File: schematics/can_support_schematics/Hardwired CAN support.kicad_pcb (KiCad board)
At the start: 2 copper layers, 39 parts, among them J1 Conn_01x05_Female, J2 Conn_01x05_Male, J3 Conn_01x05_Male, J4 Screw_Terminal_01x04, J5 Screw_Terminal_01x02, J6 Screw_Terminal_01x02, J7 Screw_Terminal_01x02, Q1 MMBF170, SW1 SW_DIP_x04, U1 SPST_POWER_RELAY, U2 PIC18F26K83, U3 MCP2562, Y1 Crystal

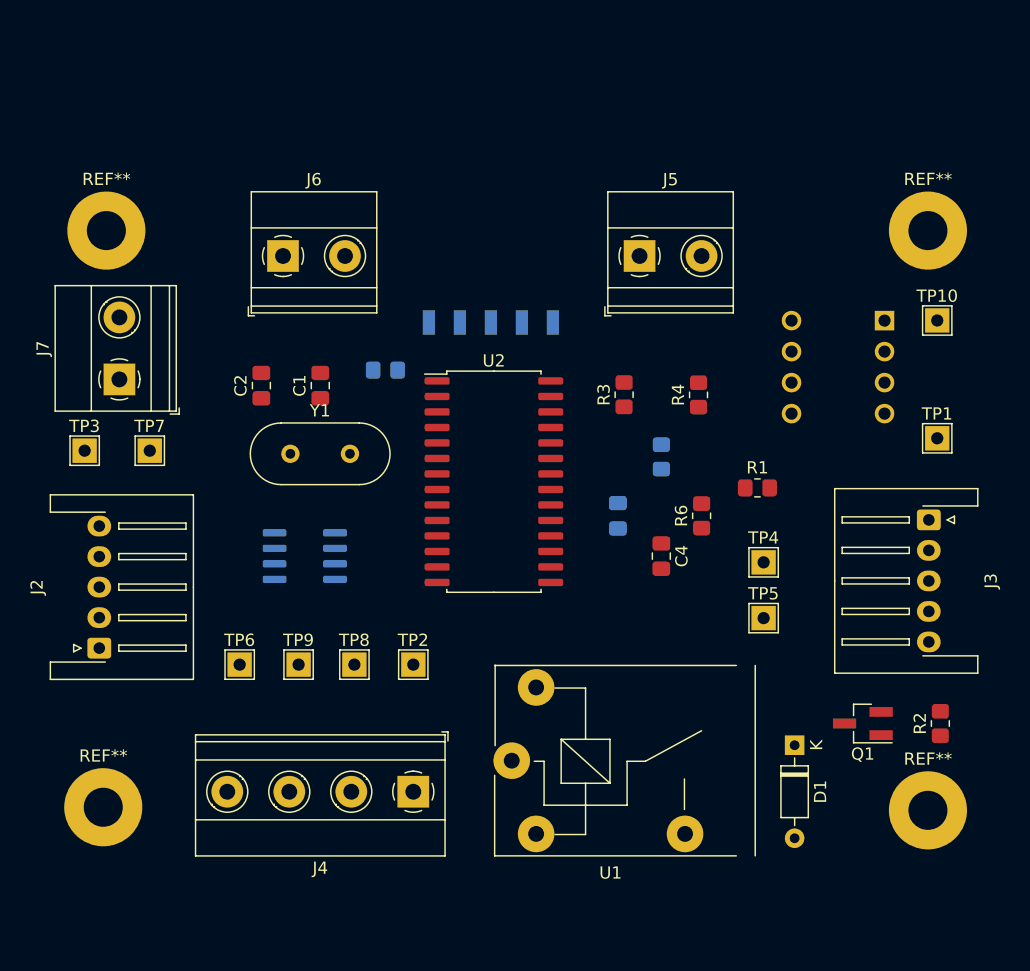
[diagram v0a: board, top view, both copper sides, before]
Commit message: Finished routing board
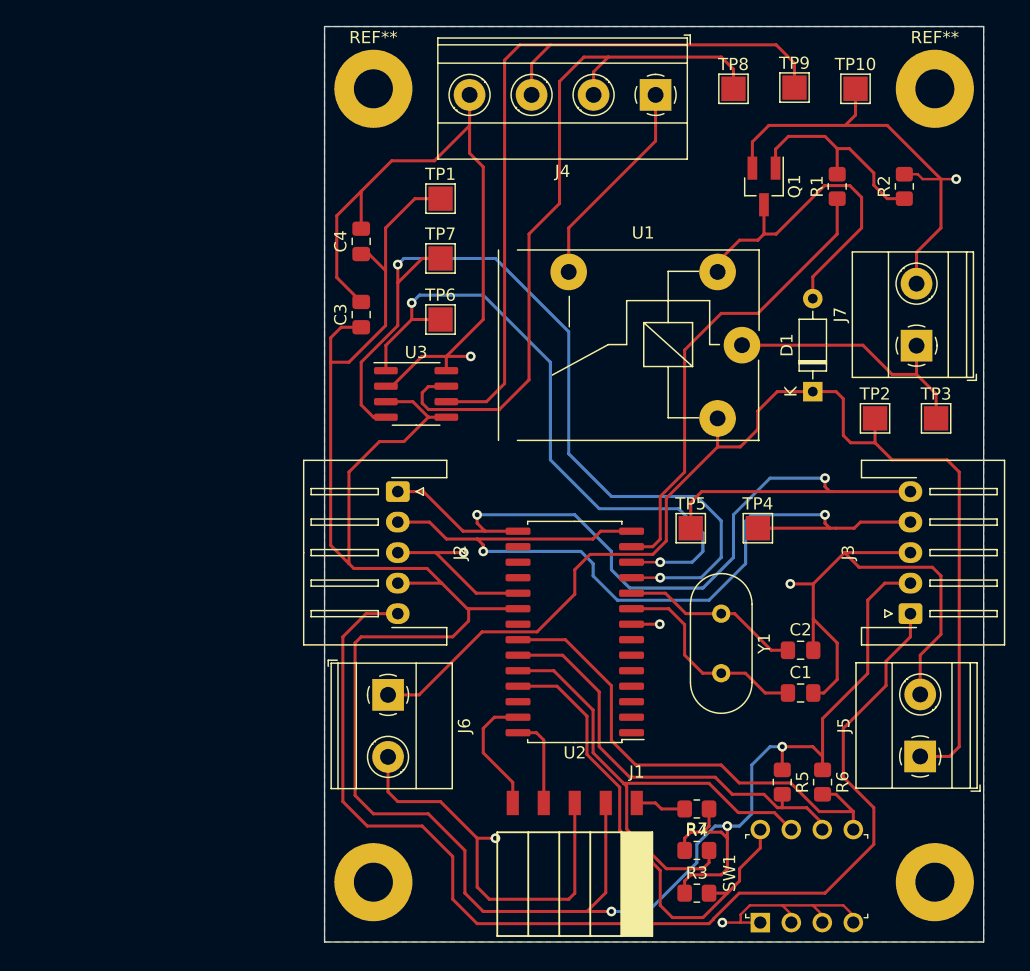
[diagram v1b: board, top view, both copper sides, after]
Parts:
- C3, J1, R5, R7, SW1, U3: moved to F.Cu
- moved TP3 69.8 mm to (171.1, 92.6)
- moved J7 65.4 mm to (169.5, 86.6)
- moved TP9 62.3 mm to (159.5, 65.5)
- moved J4 60.4 mm to (148.1, 66.1)
- moved TP8 56.5 mm to (154.5, 65.6)
- moved SW1 50.4 mm to (156.7, 133.9), turned to 90 degrees
- moved C2 49.2 mm to (160.0, 111.6), turned to 0 degrees
- moved J5 47.0 mm to (169.8, 120.3), turned to 90 degrees
- moved C1 46.7 mm to (160.0, 115.1), turned to 0 degrees
- moved TP1 45.2 mm to (130.5, 74.6)
- moved Q1 44.7 mm to (157.0, 73.6), turned to -90 degrees
- moved R2 44.1 mm to (168.5, 73.6)
- moved R7 44.1 mm to (151.5, 124.6), turned to 180 degrees
- moved TP2 42.9 mm to (166.1, 92.6)
- moved R3 41.3 mm to (151.5, 131.5), turned to 0 degrees
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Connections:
- J1 pad 1: /ICSPCLK -> /MCLR
- J1 pad 2: /ICSPDAT -> +5V
- J1 pad 4: +5V -> /ICSPDAT
- J1 pad 5: /MCLR -> /ICSPCLK
- U2 pad 13: unconnected-(U2-Pad13) -> /TRIG_PIN
- U2 pad 21: /TRIG_PIN -> unconnected-(U2-Pad21)
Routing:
- net +5V: track 0.00 -> 208.1 mm, vias 0 -> 3
- net GND: track 0.00 -> 204.9 mm, vias 0 -> 7
- net +12V: track 0.00 -> 96.0 mm
- net Net-(J2-Pad5): track 0.00 -> 93.4 mm
- net /SDA: track 0.00 -> 72.2 mm, vias 0 -> 2
- net /CAN_RX: track 0.00 -> 72.0 mm, vias 0 -> 2
- net /SCL: track 0.00 -> 70.4 mm, vias 0 -> 2
- net /CAN_L: track 0.00 -> 63.6 mm
- net /CAN_H: track 0.00 -> 59.2 mm
- net /CAN_TX: track 0.00 -> 53.4 mm, vias 0 -> 2
- net /DIP_2: track 0.00 -> 43.0 mm
- net /DIP_4: track 0.00 -> 40.5 mm
- net /DIP_1: track 0.00 -> 39.2 mm
- net /TRIG_PIN: track 0.00 -> 38.3 mm
- net /DIP_3: track 0.00 -> 34.9 mm
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- added copper zone on B.Cu, net GND
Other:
- board outline added: 54 x 75 mm

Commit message: Updated recommended changes to PCB
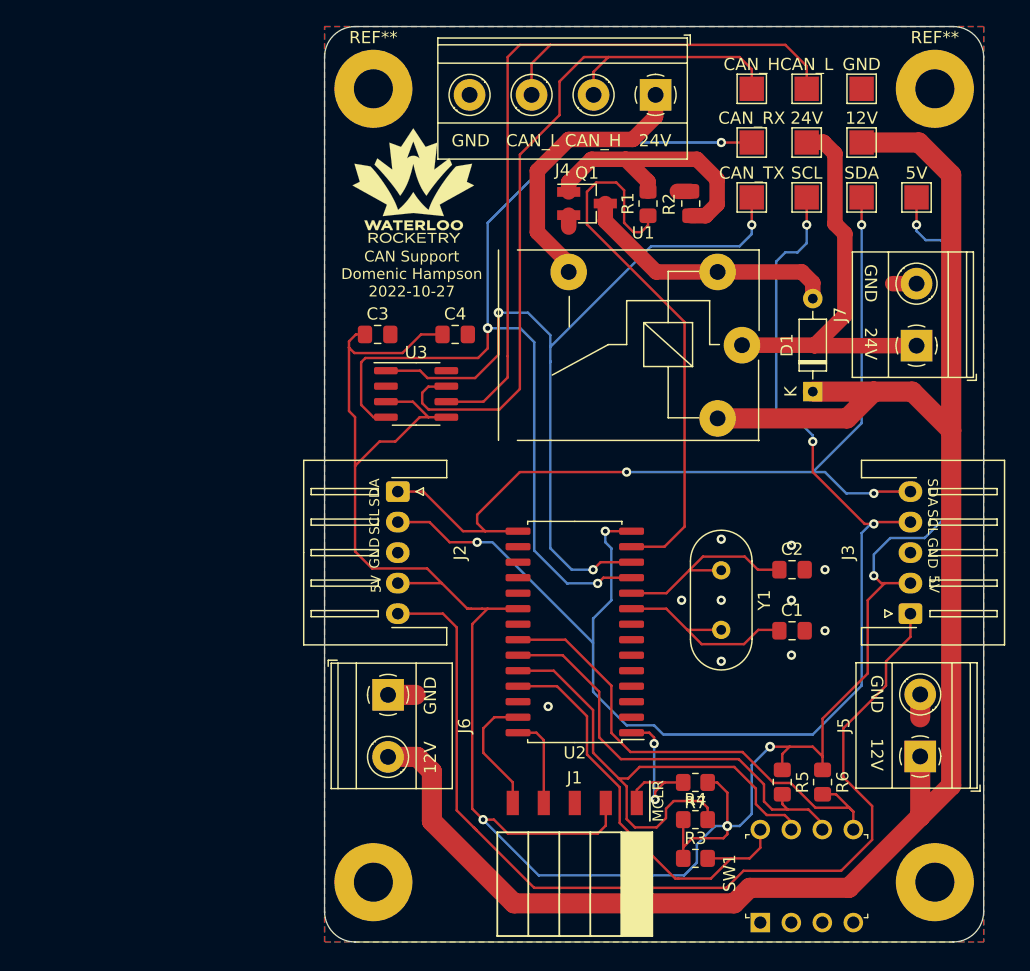
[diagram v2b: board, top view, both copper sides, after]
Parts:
- added G***: LOGO, custom:rocketry_logo_small, F.Cu at (128.3, 73.5)
- moved 5V 39.0 mm to (169.5, 74.5)
- moved SDA 30.5 mm to (165.0, 74.5)
- moved SCL 27.4 mm to (160.5, 74.5)
- moved CAN_TX 27.4 mm to (156.0, 74.5)
- moved CAN_RX 27.2 mm to (156.0, 70.0)
- moved 24V 25.0 mm to (160.5, 70.0)
- moved 12V 22.6 mm to (165.0, 70.0)
- moved R2 17.6 mm to (151.0, 75.0)
- moved R1 15.6 mm to (147.5, 75.0)
- moved Q1 14.6 mm to (142.5, 75.0), turned to 0 degrees
- moved C4 10.8 mm to (131.7, 85.7), turned to 0 degrees
- moved C2 6.64 mm to (159.3, 105.0)
- moved C1 5.15 mm to (159.3, 110.0)
- moved Y1 3.55 mm to (153.5, 105.0)
- moved R3 2.85 mm to (151.4, 128.7)
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- renumbered TP2 to 12V, TP3 to 24V, TP1 to 5V, TP8 to CAN_H, TP9 to CAN_L, TP7 to CAN_RX, TP6 to CAN_TX, TP10 to GND, TP4 to SCL, TP5 to SDA
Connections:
- net Net-(D1-Pad2) renamed /DRAIN
- net Net-(Q1-Pad1) renamed /BASE
- J6 pad 1: +12V -> GND
- J6 pad 2: GND -> +12V
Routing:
- net GND: track 204.9 -> 8.22 mm, vias 7 -> 10
- net +12V: track 96.0 -> 147.3 mm
- net /SCL: track 70.4 -> 110.9 mm, vias 2 -> 5
- net /CAN_TX: track 53.4 -> 67.2 mm, vias 2 -> 3
- net +24V: track 22.0 -> 35.3 mm
- net Net-(J2-Pad5): track 93.4 -> 80.7 mm
- net /CAN_RX: track 72.0 -> 82.1 mm, vias 2 -> 3
- net /MCLR: track 4.12 -> 14.0 mm, vias 0 -> 2
- net +5V: track 208.1 -> 200.4 mm, vias 3 -> 5
- net /TRIG_PIN: track 38.3 -> 45.4 mm
- net /DRAIN: track 28.0 -> 22.6 mm
- net /RELAY_24V: track 17.5 -> 22.7 mm
- net /BASE: track 17.3 -> 22.4 mm
- net /DIP_1: track 39.2 -> 34.4 mm
- net /SDA: track 72.2 -> 74.7 mm, vias 2 -> 3
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- added copper zone on F.Cu, net GND
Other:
- outline, holes or cut-outs redrawn
- board text added: "12V"
- board text added: "24V"
- board text added: "5V"
- board text added: "CAN Support Domenic Hampson 2022-10-27"
- board text added: "CAN_H"
- board text added: "CAN_L"
- board text added: "GND"
- board text added: "SCL"
- board text added: "SDA"
- board text added: "~{MCLR}"

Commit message: Updated PCB according to recommended changes
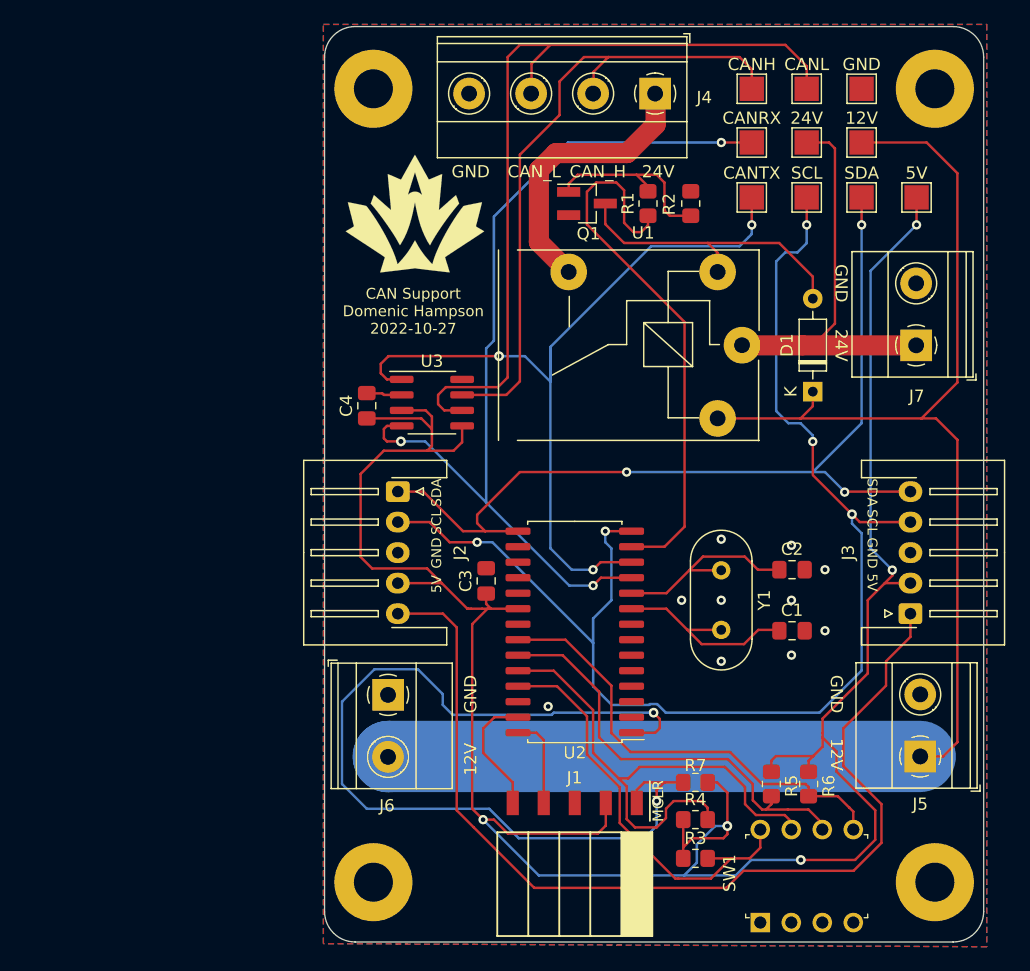
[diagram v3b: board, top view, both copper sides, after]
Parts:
- removed the G*** at (128.3, 73.5)
- removed the REF** at (171.0, 65.6)
- removed the REF** at (125.0, 65.6)
- added ?: , , F.Cu at (171.0, 65.6)
- added ?: , , F.Cu at (125.0, 65.6)
- added G***: LOGO, custom:rocketry_logo_small_noletters, F.Cu at (128.4, 75.8)
- moved C3 22.1 mm to (134.2, 105.9), turned to 90 degrees
- moved C4 9.30 mm to (124.5, 91.6), turned to 90 degrees
- moved U3 1.48 mm to (129.8, 91.3)
- moved R6 1.16 mm to (160.7, 122.6)
- moved R5 0.91 mm to (157.6, 122.6)
- moved J4 0.12 mm to (148.1, 66.0)
- renumbered CAN_H to CANH, CAN_L to CANL, CAN_RX to CANRX, CAN_TX to CANTX
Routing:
- net /MCLR: track 14.0 -> 76.4 mm
- net +12V: track 147.3 -> 125.1 mm
- net /CAN_H: track 60.7 -> 53.3 mm
- net /BASE: track 22.4 -> 15.5 mm
- net /CAN_RX: track 82.1 -> 75.2 mm
- net GND: track 8.22 -> 2.92 mm
- net /CAN_L: track 64.4 -> 67.7 mm
- net /DIP_4: track 40.2 -> 37.5 mm
- net /DRAIN: track 22.6 -> 25.0 mm
- net /SCL: track 110.9 -> 109.0 mm
- net +5V: track 200.4 -> 202.2 mm
- net /CAN_TX: track 67.2 -> 68.1 mm
- net Net-(J2-Pad5): track 80.7 -> 81.6 mm
- net +24V: track 35.3 -> 34.5 mm
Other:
- outline, holes or cut-outs redrawn

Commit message: Updated Board
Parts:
- moved C3 1.93 mm to (132.5, 105.2)
- moved U3 1.27 mm to (131.1, 91.3)
- moved C4 0.25 mm to (124.2, 91.6)
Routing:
- net Net-(J2-Pad5): track 81.6 -> 55.3 mm
- net /SCL: track 109.0 -> 89.4 mm, vias 5 -> 4
- net +5V: track 202.2 -> 212.4 mm
- net /MCLR: track 76.4 -> 70.9 mm
- net /TRIG_PIN: track 45.4 -> 42.3 mm
- net GND: track 2.92 -> 0.03 mm, vias 10 -> 9
- net /CAN_L: track 67.7 -> 65.8 mm
- net /SDA: track 74.6 -> 76.5 mm, vias 3 -> 4
- net /CAN_TX: track 68.1 -> 66.5 mm
- net /CAN_H: track 53.3 -> 52.0 mm
- net /CAN_RX: track 75.2 -> 76.0 mm
